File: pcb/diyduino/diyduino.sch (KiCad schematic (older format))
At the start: 38 parts, among them J1 Conn_Coaxial_Power, U1 ATMEGA328-PU, U2 L7805, Y1 16MHz

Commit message: Reworked the ditduino.
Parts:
- removed A0, A1, A2, A3, A4, A5, D10, DA2, DA3, DA4, DA5, DA6, DA7, DA8, DA9, MISO1, MOSI1, RXD1, SCK1, SCL1, SDA1, TXD1: DATA, Pin_Headers:Pin_Header_Straight_1x03_Pitch2.54mm, symbol DATA
- removed J1: Conn_Coaxial_Power, Connectors:BARREL_JACK, symbol Conn_Coaxial_Power
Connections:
- net labels removed: A6, A7
- wire segments 53 -> 24

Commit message: Reworked diyduino module.
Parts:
- added D1, D2: D, Diodes_THT:D_T-1_P5.08mm_Horizontal, symbol D
- LED3: footprint LEDs:LED_D3.0mm -> LEDs:LED_Rectangular_W3.0mm_H2.0mm
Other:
- moved on the sheet: C5, LED3, PR2
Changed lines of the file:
@@
 L R PR2
 U 1 1 5AC0021E
-P 3500 4350
-F 0 "PR2" V 3580 4350 50  0000 C CNN
-F 1 "R" V 3500 4350 50  0000 C CNN
-F 2 "Resistors_THT:R_Axial_DIN0204_L3.6mm_D1.6mm_P7.62mm_Horizontal" V 3430 4350 50  0001 C CNN
-F 3 "" H 3500 4350 50  0001 C CNN
-	1    3500 4350
+P 3800 4350
+F 0 "PR2" V 3880 4350 50  0000 C CNN
+F 1 "R" V 3800 4350 50  0000 C CNN
+F 2 "Resistors_THT:R_Axial_DIN0204_L3.6mm_D1.6mm_P7.62mm_Horizontal" V 3730 4350 50  0001 C CNN
+F 3 "" H 3800 4350 50  0001 C CNN
+	1    3800 4350
 	-1   0    0    1
 $EndComp
@@
 L LED LED3
 U 1 1 5AC002AF
-P 3500 4650
-F 0 "LED3" H 3500 4750 50  0000 C CNN
-F 1 "POWER" H 3500 4550 50  0000 C CNN
-F 2 "LEDs:LED_D3.0mm" H 3500 4650 50  0001 C CNN
-F 3 "" H 3500 4650 50  0001 C CNN
-	1    3500 4650
+P 3800 4650
+F 0 "LED3" H 3800 4750 50  0000 C CNN
+F 1 "POWER" H 3800 4550 50  0000 C CNN
+F 2 "LEDs:LED_Rectangular_W3.0mm_H2.0mm" H 3800 4650 50  0001 C CNN
+F 3 "" H 3800 4650 50  0001 C CNN
+	1    3800 4650
 	0    -1   -1   0
 $EndComp
-Text Label 3350 4200 2    60   ~ 0
+Text Label 3500 4200 0    60   ~ 0
 VCC
 $Comp
@@
 Text Label 5350 5800 2    60   ~ 0
 A5
-Text Label 2300 5300 0    60   ~ 0
+Text Label 2600 5300 0    60   ~ 0
 VCC
 $Comp
@@
 L C C5
 U 1 1 5AC3FB72
-P 3100 4350
-F 0 "C5" H 3125 4450 50  0000 L CNN
-F 1 "100nF" H 3125 4250 50  0000 L CNN
-F 2 "Capacitors_THT:CP_Radial_D6.3mm_P2.50mm" H 3138 4200 50  0001 C CNN
-F 3 "" H 3100 4350 50  0001 C CNN
-	1    3100 4350
+P 3400 4350
+F 0 "C5" H 3425 4450 50  0000 L CNN
+F 1 "100nF" H 3425 4250 50  0000 L CNN
+F 2 "Capacitors_THT:CP_Radial_D6.3mm_P2.50mm" H 3438 4200 50  0001 C CNN
+F 3 "" H 3400 4350 50  0001 C CNN
+	1    3400 4350
 	1    0    0    -1
 $EndComp
@@
 	4200 1700 4200 1750
 Wire Wire Line
-	3100 4200 3500 4200
-Wire Wire Line
 	2800 4500 2800 4800
 Wire Wire Line
-	2500 4800 3500 4800
-Wire Wire Line
-	3100 4500 3100 4800
-Connection ~ 3100 4800
+	2500 4800 3800 4800
 Wire Wire Line
 	2500 4500 2500 4800
 Connection ~ 2800 4800
+$Comp
+L D D1
+U 1 1 5AC4FB56
+P 2450 5300
+F 0 "D1" H 2450 5400 50  0000 C CNN
+F 1 "D" H 2450 5200 50  0000 C CNN
+F 2 "Diodes_THT:D_T-1_P5.08mm_Horizontal" H 2450 5300 50  0001 C CNN
+F 3 "" H 2450 5300 50  0001 C CNN
+	1    2450 5300
+	-1   0    0    1
+$EndComp
+$Comp
+L D D2
+U 1 1 5AC4FCDF
+P 3250 4200
+F 0 "D2" H 3250 4300 50  0000 C CNN
+F 1 "D" H 3250 4100 50  0000 C CNN
+F 2 "Diodes_THT:D_T-1_P5.08mm_Horizontal" H 3250 4200 50  0001 C CNN
+F 3 "" H 3250 4200 50  0001 C CNN
+	1    3250 4200
+	-1   0    0    1
+$EndComp
+Wire Wire Line
+	3800 4200 3400 4200
+Wire Wire Line
+	3400 4500 3400 4800
+Connection ~ 3400 4800
 $EndSCHEMATC

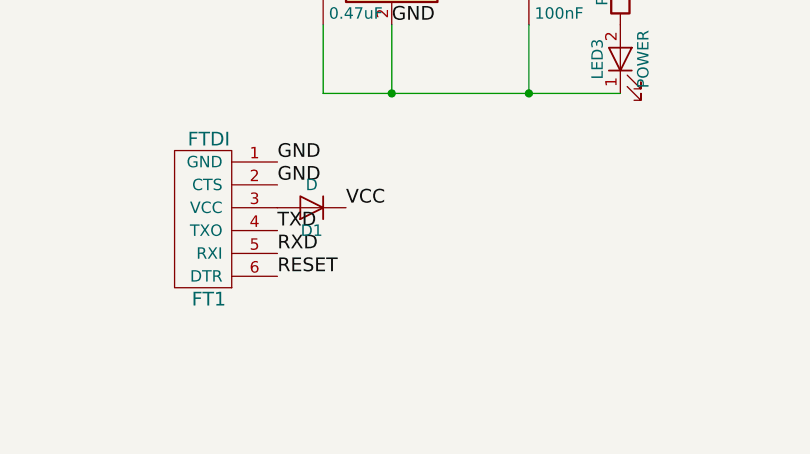
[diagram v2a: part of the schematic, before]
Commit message: Added an extra FTDI header, with the RX and TX reversed.
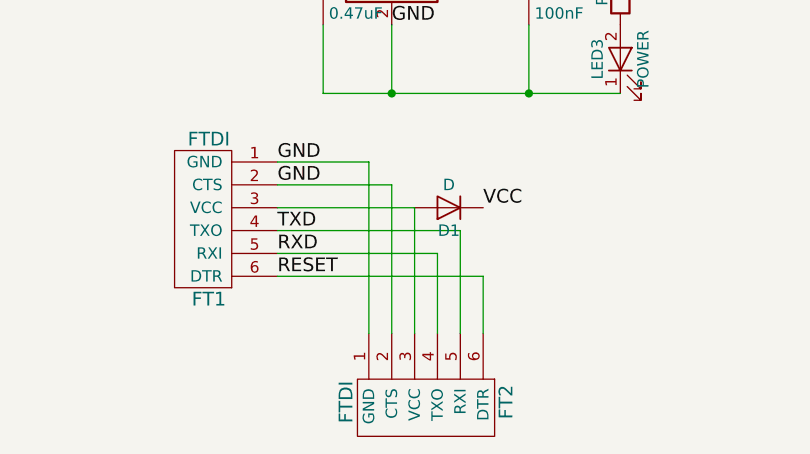
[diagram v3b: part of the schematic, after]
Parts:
- added FT2: FTDI, Pin_Headers:Pin_Header_Straight_1x06_Pitch2.54mm, symbol FTDI
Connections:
- wire segments 24 -> 36
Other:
- moved on the sheet: D1
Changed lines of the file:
@@
 Text Label 5350 5800 2    60   ~ 0
 A5
-Text Label 2600 5300 0    60   ~ 0
+Text Label 3200 5300 0    60   ~ 0
 VCC
 $Comp
@@
 L D D1
 U 1 1 5AC4FB56
-P 2450 5300
-F 0 "D1" H 2450 5400 50  0000 C CNN
-F 1 "D" H 2450 5200 50  0000 C CNN
-F 2 "Diodes_THT:D_T-1_P5.08mm_Horizontal" H 2450 5300 50  0001 C CNN
-F 3 "" H 2450 5300 50  0001 C CNN
-	1    2450 5300
+P 3050 5300
+F 0 "D1" H 3050 5400 50  0000 C CNN
+F 1 "D" H 3050 5200 50  0000 C CNN
+F 2 "Diodes_THT:D_T-1_P5.08mm_Horizontal" H 3050 5300 50  0001 C CNN
+F 3 "" H 3050 5300 50  0001 C CNN
+	1    3050 5300
 	-1   0    0    1
 $EndComp
@@
 	3400 4500 3400 4800
 Connection ~ 3400 4800
+$Comp
+L FTDI FT2
+U 1 1 5AC50B3D
+P 2950 6150
+F 0 "FT2" H 2950 5800 60  0000 C CNN
+F 1 "FTDI" H 2950 6500 60  0000 C CNN
+F 2 "Pin_Headers:Pin_Header_Straight_1x06_Pitch2.54mm" H 2950 6150 60  0001 C CNN
+F 3 "" H 2950 6150 60  0001 C CNN
+	1    2950 6150
+	0    -1   -1   0
+$EndComp
+Wire Wire Line
+	2300 5600 3200 5600
+Wire Wire Line
+	3200 5600 3200 5850
+Wire Wire Line
+	2300 5100 2700 5100
+Wire Wire Line
+	2700 5100 2700 5850
+Wire Wire Line
+	2300 5200 2800 5200
+Wire Wire Line
+	2800 5200 2800 5850
+Wire Wire Line
+	2300 5300 2900 5300
+Wire Wire Line
+	2900 5300 2900 5850
+Wire Wire Line
+	2300 5400 3100 5400
+Wire Wire Line
+	3100 5400 3100 5850
+Wire Wire Line
+	2300 5500 3000 5500
+Wire Wire Line
+	3000 5500 3000 5850
 $EndSCHEMATC

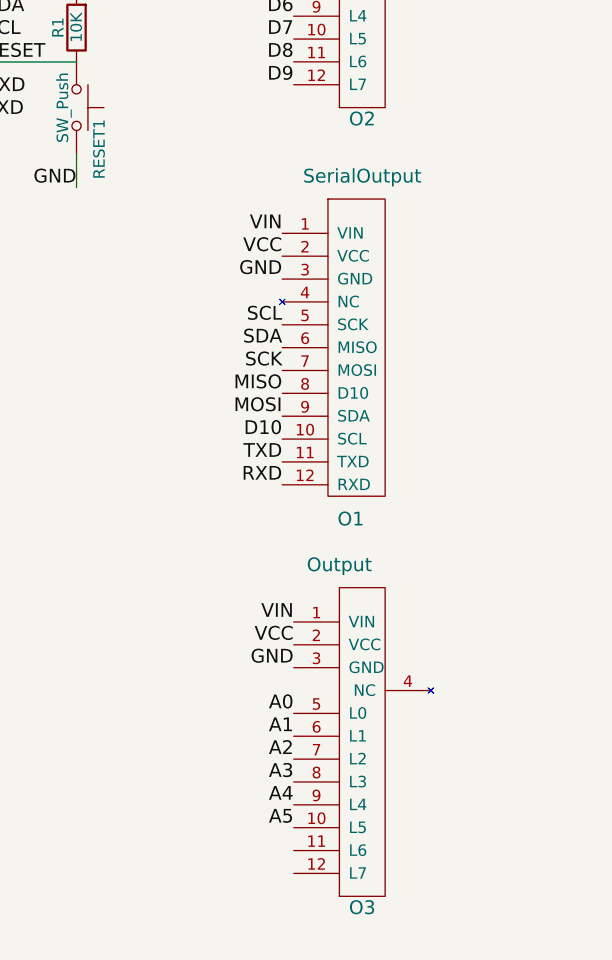
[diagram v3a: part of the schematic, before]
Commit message: Reordered serial connectors so that A4 and A5 on the analog connector are in the same place as they are on the serial connector.
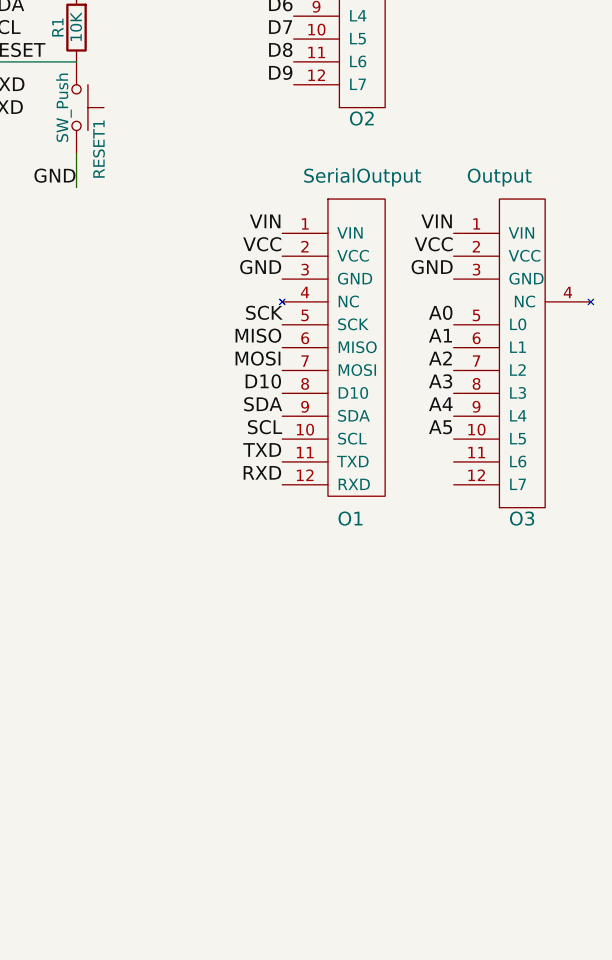
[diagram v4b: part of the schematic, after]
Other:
- moved on the sheet: O3
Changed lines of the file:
@@
 L Output O3
 U 1 1 5AC3A8AB
-P 5650 4600
-F 0 "O3" H 5650 3050 60  0000 C CNN
-F 1 "Output" H 5550 4550 60  0000 C CNN
-F 2 "Socket_Strips:Socket_Strip_Straight_1x12_Pitch2.54mm" H 5700 4550 60  0001 C CNN
-F 3 "" H 5700 4550 60  0001 C CNN
-	1    5650 4600
+P 6350 2900
+F 0 "O3" H 6350 1350 60  0000 C CNN
+F 1 "Output" H 6250 2850 60  0000 C CNN
+F 2 "Socket_Strips:Socket_Strip_Straight_1x12_Pitch2.54mm" H 6400 2850 60  0001 C CNN
+F 3 "" H 6400 2850 60  0001 C CNN
+	1    6350 2900
 	1    0    0    -1
 $EndComp
@@
 Text Label 5300 3400 2    60   ~ 0
 GND
+Text Label 5300 4100 2    60   ~ 0
+SCL
+Text Label 5300 4000 2    60   ~ 0
+SDA
 Text Label 5300 3600 2    60   ~ 0
-SCL
+SCK
 Text Label 5300 3700 2    60   ~ 0
-SDA
+MISO
 Text Label 5300 3800 2    60   ~ 0
-SCK
+MOSI
 Text Label 5300 3900 2    60   ~ 0
-MISO
-Text Label 5300 4000 2    60   ~ 0
-MOSI
-Text Label 5300 4100 2    60   ~ 0
 D10
 Text Label 5300 4200 2    60   ~ 0
@@
 Text Label 5300 4300 2    60   ~ 0
 RXD
-Text Label 5350 4900 2    60   ~ 0
+Text Label 6050 3200 2    60   ~ 0
 VIN
-Text Label 5350 5000 2    60   ~ 0
+Text Label 6050 3300 2    60   ~ 0
 VCC
-Text Label 5350 5100 2    60   ~ 0
+Text Label 6050 3400 2    60   ~ 0
 GND
-Text Label 5350 5300 2    60   ~ 0
+Text Label 6050 3600 2    60   ~ 0
 A0
-Text Label 5350 5400 2    60   ~ 0
+Text Label 6050 3700 2    60   ~ 0
 A1
-Text Label 5350 5500 2    60   ~ 0
+Text Label 6050 3800 2    60   ~ 0
 A2
-Text Label 5350 5600 2    60   ~ 0
+Text Label 6050 3900 2    60   ~ 0
 A3
-Text Label 5350 5700 2    60   ~ 0
+Text Label 6050 4000 2    60   ~ 0
 A4
-Text Label 5350 5800 2    60   ~ 0
+Text Label 6050 4100 2    60   ~ 0
 A5
 Text Label 3200 5300 0    60   ~ 0
